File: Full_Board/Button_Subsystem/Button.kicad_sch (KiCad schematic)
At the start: 7 parts

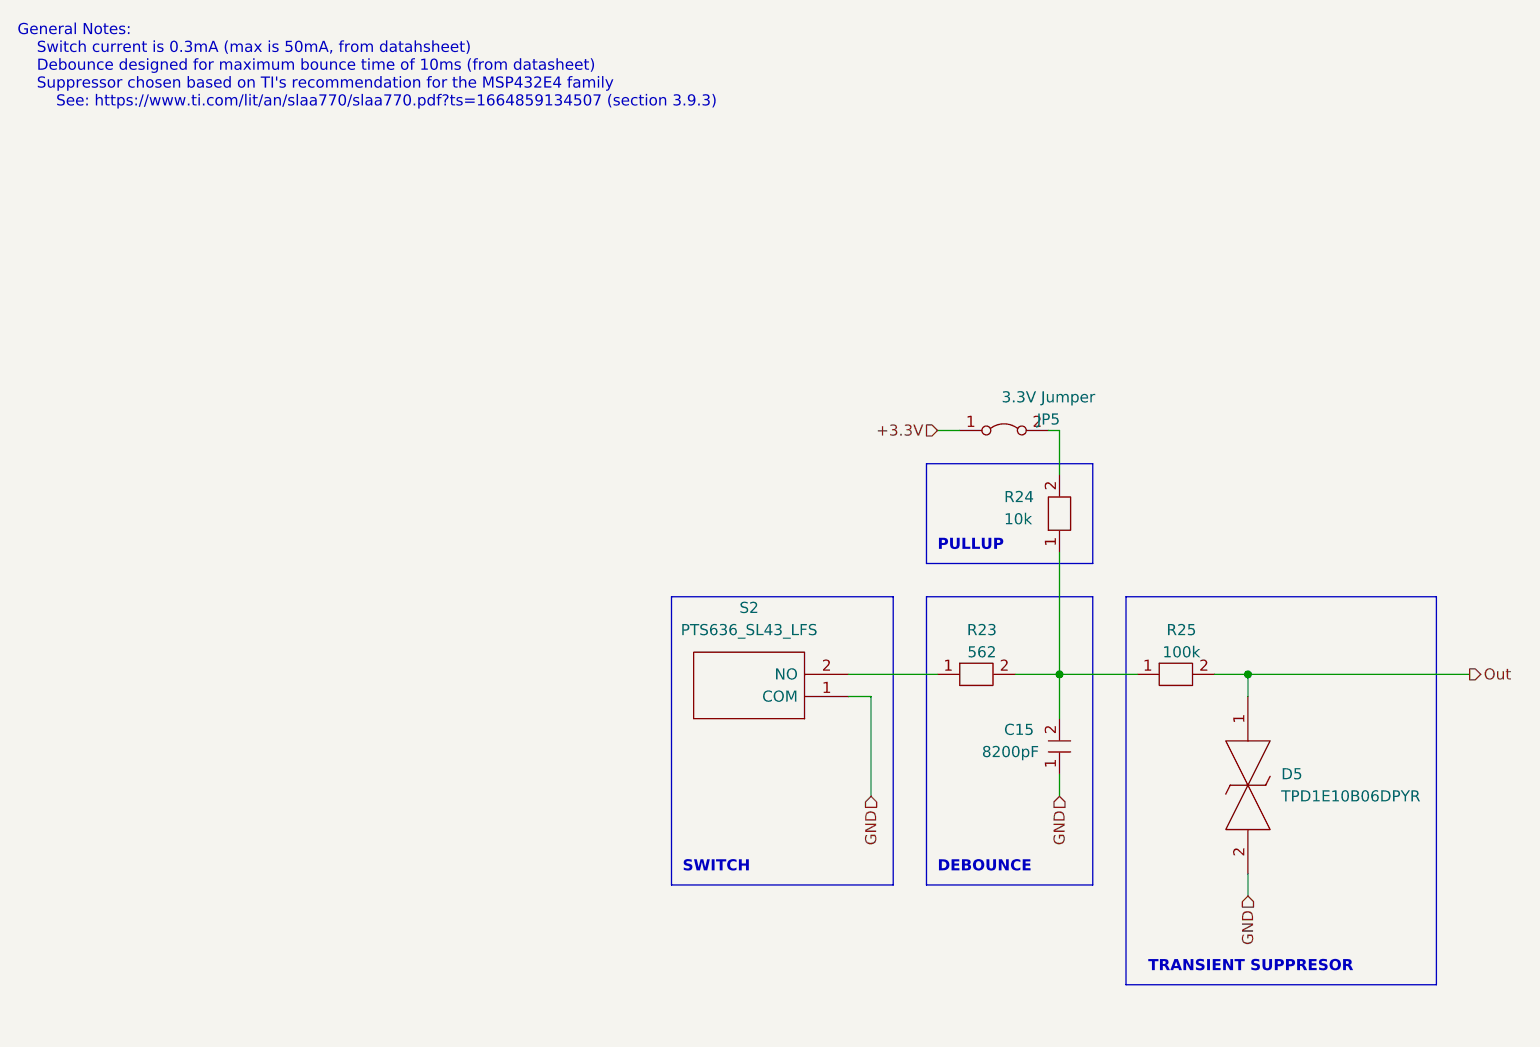
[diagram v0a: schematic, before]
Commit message: Swapped TVS Diodes
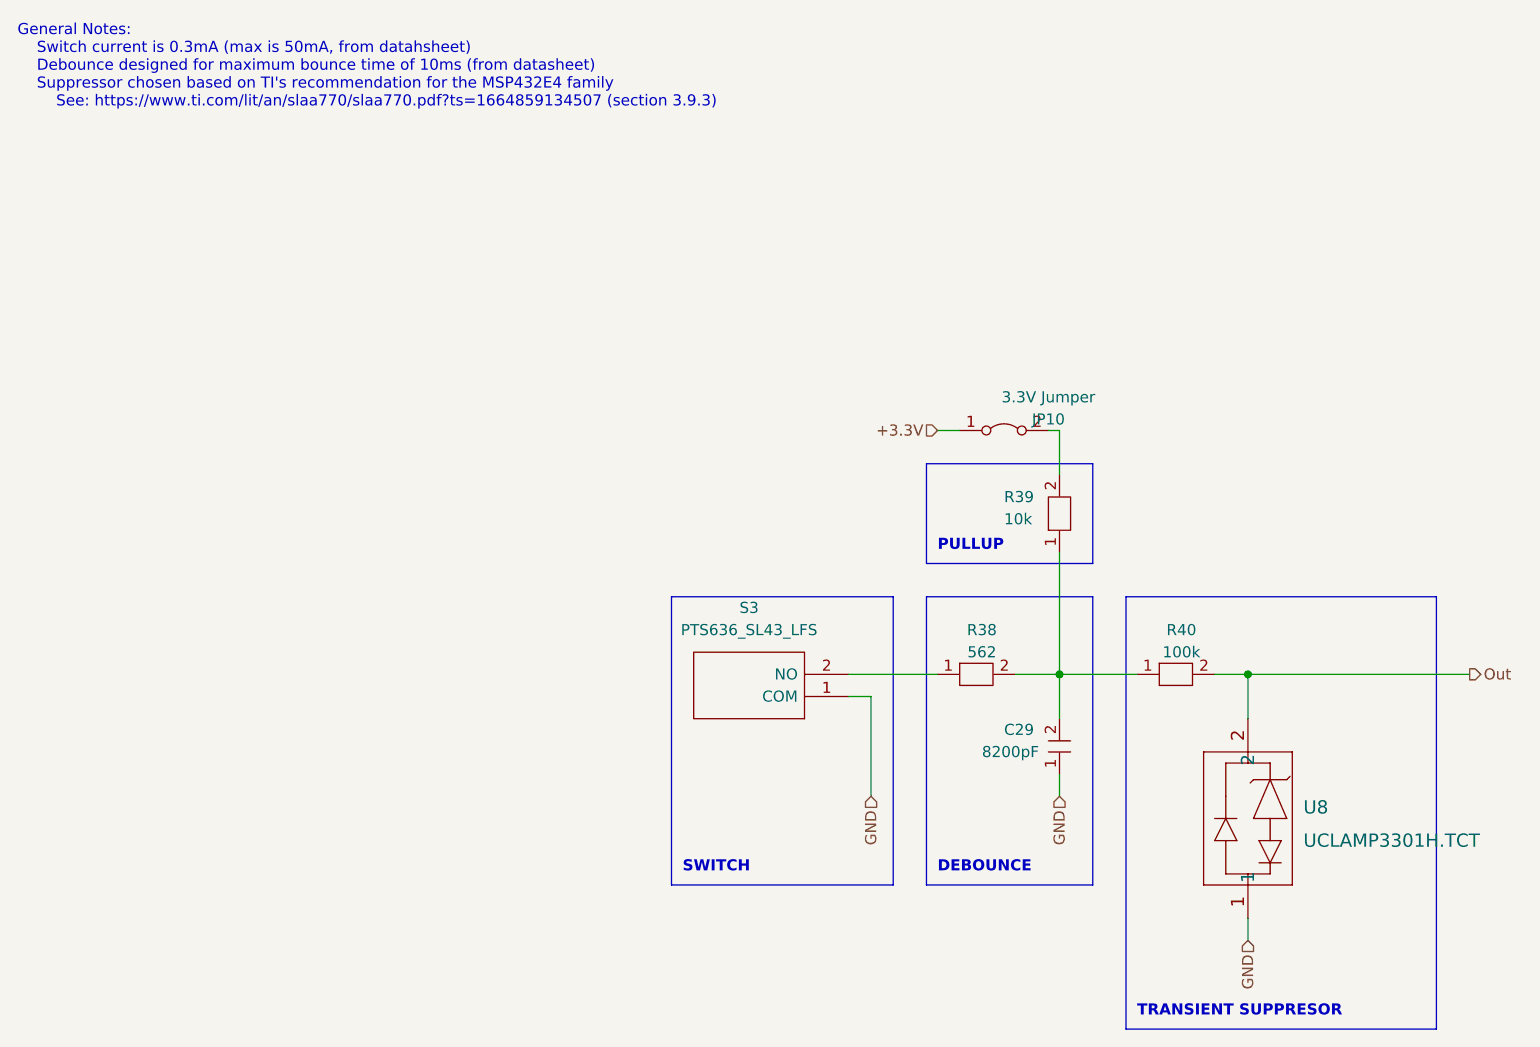
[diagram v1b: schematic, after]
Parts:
- removed D5: TPD1E10B06DPYR, TPD1E10B06DPYR:TPD1E10B06DPYR, symbol TPD1E10B06DPYR:TPD1E10B06DPYR
- added U8: UCLAMP3301H.TCT, SOD_01H.TCT_SEM, symbol UCLAMP3301H-TCT:UCLAMP3301H.TCT
- renumbered C15 to C29, JP5 to JP10, R23 to R38, R24 to R39, R25 to R40, S2 to S3
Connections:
- net GND: now also U8.1
- net Out: now also U8.2
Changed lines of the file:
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@@
     (stroke (width 0) (type default) (color 0 0 0 0))
   )
-  (polyline (pts (xy 180.34 129.54) (xy 180.34 85.09))
+  (polyline (pts (xy 180.34 134.62) (xy 180.34 85.09))
     (stroke (width 0) (type default) (color 0 0 0 0))
   )
@@
     (stroke (width 0) (type default) (color 0 0 0 0))
   )
-  (wire (pts (xy 158.75 93.98) (xy 158.75 96.52))
+  (wire (pts (xy 158.75 93.98) (xy 158.75 99.06))
     (stroke (width 0) (type default) (color 0 0 0 0))
   )
@@
     (stroke (width 0) (type default) (color 0 0 0 0))
   )
-  (polyline (pts (xy 144.78 129.54) (xy 180.34 129.54))
+  (polyline (pts (xy 144.78 134.62) (xy 180.34 134.62))
     (stroke (width 0) (type default) (color 0 0 0 0))
   )
@@
     (stroke (width 0) (type default) (color 0 0 0 0))
   )
+  (wire (pts (xy 158.75 121.92) (xy 158.75 124.46))
+    (stroke (width 0) (type default) (color 0 0 0 0))
+  )
   (polyline (pts (xy 92.71 118.11) (xy 118.11 118.11))
     (stroke (width 0) (type default) (color 0 0 0 0))
@@
     (stroke (width 0) (type default) (color 0 0 0 0))
   )
-  (polyline (pts (xy 144.78 85.09) (xy 144.78 129.54))
+  (polyline (pts (xy 144.78 85.09) (xy 144.78 134.62))
     (stroke (width 0) (type default) (color 0 0 0 0))
   )
@@
     (stroke (width 0) (type default) (color 0 0 0 0))
   )
-  (wire (pts (xy 158.75 116.84) (xy 158.75 119.38))
-    (stroke (width 0) (type default) (color 0 0 0 0))
-  )
-  (text "TRANSIENT SUPPRESOR" (at 147.32 128.27 0)
+  (text "TRANSIENT SUPPRESOR" (at 146.05 133.35 0)
     (effects (font (size 1.27 1.27) bold) (justify left bottom))
   )
@@
     (effects (font (size 1.27 1.27)) (justify right))
   )
-  (hierarchical_label "GND" (shape input) (at 158.75 119.38 270)
+  (hierarchical_label "GND" (shape input) (at 158.75 124.46 270)
     (effects (font (size 1.27 1.27)) (justify right))
   )
@@
   (symbol (lib_id "RMCF1206FT10K0:10k") (at 137.16 80.01 90)
     (in_bom yes) (on_board yes)
-    (property "Reference" "R24" (id 0) (at 130.81 73.66 90)
+    (property "Reference" "R39" (id 0) (at 130.81 73.66 90)
       (effects (font (size 1.27 1.27)) (justify right))
     )
@@
   (symbol (lib_id "C1210C822K2RACAUTO:C1210C822K2RACAUTO") (at 137.16 105.41 90)
     (in_bom yes) (on_board yes)
-    (property "Reference" "C15" (id 0) (at 130.81 100.33 90)
+    (property "Reference" "C29" (id 0) (at 130.81 100.33 90)
       (effects (font (size 1.27 1.27)) (justify right))
     )
@@
     (pin "2")
   )
+  (symbol (lib_id "UCLAMP3301H-TCT:UCLAMP3301H.TCT") (at 158.75 130.81 90)
+    (in_bom yes) (on_board yes) (fields_autoplaced)
+    (property "Reference" "U8" (id 0) (at 165.1 109.22 90)
+      (effects (font (size 1.524 1.524)) (justify right))
+    )
+    (property "Value" "UCLAMP3301H.TCT" (id 1) (at 165.1 113.03 90)
+      (effects (font (size 1.524 1.524)) (justify right))
+    )
+    (property "Footprint" "SOD_01H.TCT_SEM" (id 2) (at 152.654 110.49 0)
+      (effects (font (size 1.524 1.524)) hide)
+    )
+    (property "Datasheet" "https://semtech.my.salesforce.com/sfc/p/#E0000000JelG/a/44000000MDWf/s0KJxyOHQyYOcvBXVBK9X3X8Cxj1gNltZ2vd2k1S0Wo" (id 3) (at 158.75 130.81 0)
+      (effects (font (size 1.524 1.524)) hide)
+    )
+    (property "Manufacturers Part Number" "UCLAMP3301H.TCT" (id 4) (at 158.75 130.81 0)
+      (effects (font (size 1.27 1.27)) hide)
+    )
+    (property "Digikey Part Number" "UCLAMP3301HDKR-ND" (id 5) (at 158.75 130.81 0)
+      (effects (font (size 1.27 1.27)) hide)
+    )
+    (property "Mouser Part Number" "" (id 6) (at 158.75 130.81 0)
+      (effects (font (size 1.27 1.27)) hide)
+    )
+    (property "Digikey Link" "https://www.digikey.com/en/products/detail/semtech-corporation/UCLAMP3301H-TCT/1000952" (id 7) (at 158.75 130.81 0)
+      (effects (font (size 1.27 1.27)) hide)
+    )
+    (property "Mouser Link" "" (id 8) (at 158.75 130.81 0)
+      (effects (font (size 1.27 1.27)) hide)
+    )
+    (pin "1")
+    (pin "2")
+  )
   (symbol (lib_id "Jumper:Jumper_2_Bridged") (at 130.81 66.04 0)
     (in_bom yes) (on_board yes)
-    (property "Reference" "JP5" (id 0) (at 135.89 64.77 0))
+    (property "Reference" "JP10" (id 0) (at 135.89 64.77 0))
     (property "Value" "3.3V Jumper" (id 1) (at 135.89 62.23 0))
     (property "Footprint" "TestPoint:TestPoint_2Pads_Pitch2.54mm_Drill0.8mm" (id 2) (at 130.81 66.04 0)
@@
   (symbol (lib_id "CR0402-FX-5620GLF:CR0402-FX-5620GLF") (at 123.19 93.98 0)
     (in_bom yes) (on_board yes)
-    (property "Reference" "R23" (id 0) (at 128.27 88.9 0))
+    (property "Reference" "R38" (id 0) (at 128.27 88.9 0))
     (property "Value" "562" (id 1) (at 128.27 91.44 0))
     (property "Footprint" "CR0402-FX-5620GLF:RESC1005X40N" (id 2) (at 137.16 92.71 0)
@@
   (symbol (lib_id "RCV2512100KFKEGAT:RCV2512100KFKEGAT") (at 146.05 93.98 0)
     (in_bom yes) (on_board yes)
-    (property "Reference" "R25" (id 0) (at 151.13 88.9 0))
+    (property "Reference" "R40" (id 0) (at 151.13 88.9 0))
     (property "Value" "100k" (id 1) (at 151.13 91.44 0))
     (property "Footprint" "RCV2512100KFKEGAT:RESC6332X70N" (id 2) (at 160.02 92.71 0)
@@
   (symbol (lib_id "PTS636_SL43_LFS:PTS636_SL43_LFS") (at 113.03 96.52 180)
     (in_bom yes) (on_board yes) (fields_autoplaced)
-    (property "Reference" "S2" (id 0) (at 101.6 86.36 0))
+    (property "Reference" "S3" (id 0) (at 101.6 86.36 0))
     (property "Value" "PTS636_SL43_LFS" (id 1) (at 101.6 88.9 0))
     (property "Footprint" "PTS636_SL43_LFS:PTS636SL43LFS" (id 2) (at 93.98 99.06 0)
@@
     )
     (pin "1")
-    (pin "2")
-  )
-  (symbol (lib_id "TPD1E10B06DPYR:TPD1E10B06DPYR") (at 158.75 96.52 270)
-    (in_bom yes) (on_board yes)
-    (property "Reference" "D5" (id 0) (at 162.56 105.41 90)
-      (effects (font (size 1.27 1.27)) (justify left))
-    )
-    (property "Value" "TPD1E10B06DPYR" (id 1) (at 162.56 107.9499 90)
-      (effects (font (size 1.27 1.27)) (justify left))
-    )
-    (property "Footprint" "TPD1E10B06DPYR:TPD1E10B06DPYR" (id 2) (at 162.56 109.22 0)
-      (effects (font (size 1.27 1.27)) (justify left bottom) hide)
-    )
-    (property "Datasheet" "https://www.ti.com/lit/ds/symlink/tpd1e10b06.pdf?HQS=dis-mous-null-mousermode-dsf-pf-null-wwe&ts=1664782336823&ref_url=https%253A%252F%252Feu.mouser.com%252F" (id 3) (at 160.02 109.22 0)
-      (effects (font (size 1.27 1.27)) (justify left bottom) hide)
-    )
-    (property "Manufacturer's Part Number" "TPD1E10B06DPYR" (id 4) (at 144.78 109.22 0)
-      (effects (font (size 1.27 1.27)) (justify left bottom) hide)
-    )
-    (property "Digikey Part Number" "296-30406-1-ND" (id 5) (at 157.48 109.22 0)
-      (effects (font (size 1.27 1.27)) (justify left bottom) hide)
-    )
-    (property "Mouser Part Number" "595-TPD1E10B06DPYR" (id 6) (at 152.4 109.22 0)
-      (effects (font (size 1.27 1.27)) (justify left bottom) hide)
-    )
-    (property "Digikey link" "https://www.digikey.com/en/products/detail/texas-instruments/TPD1E10B06DPYR/3197744" (id 7) (at 149.86 109.22 0)
-      (effects (font (size 1.27 1.27)) (justify left bottom) hide)
-    )
-    (property "Mouser link" "https://www.mouser.com/ProductDetail/Texas-Instruments/TPD1E10B06DPYR?qs=UFc95S4Z4CaJYpQ4xqTc0g%3D%3D" (id 8) (at 147.32 109.22 0)
-      (effects (font (size 1.27 1.27)) (justify left bottom) hide)
-    )
-    (pin "1")

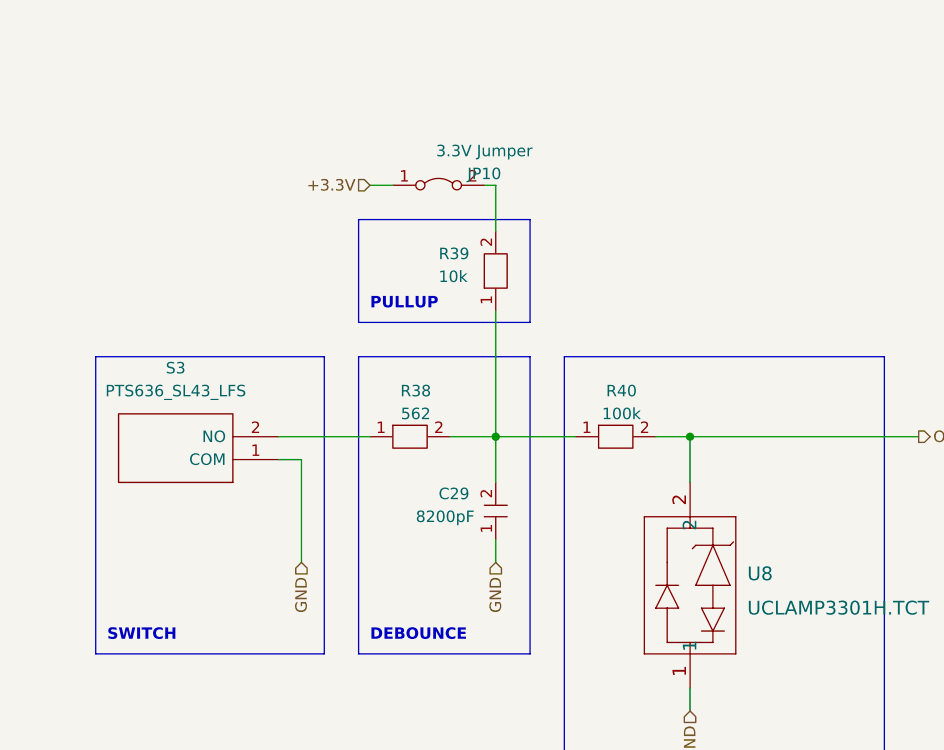
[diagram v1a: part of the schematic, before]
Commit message: Relayed out the power supply and stepper drivers
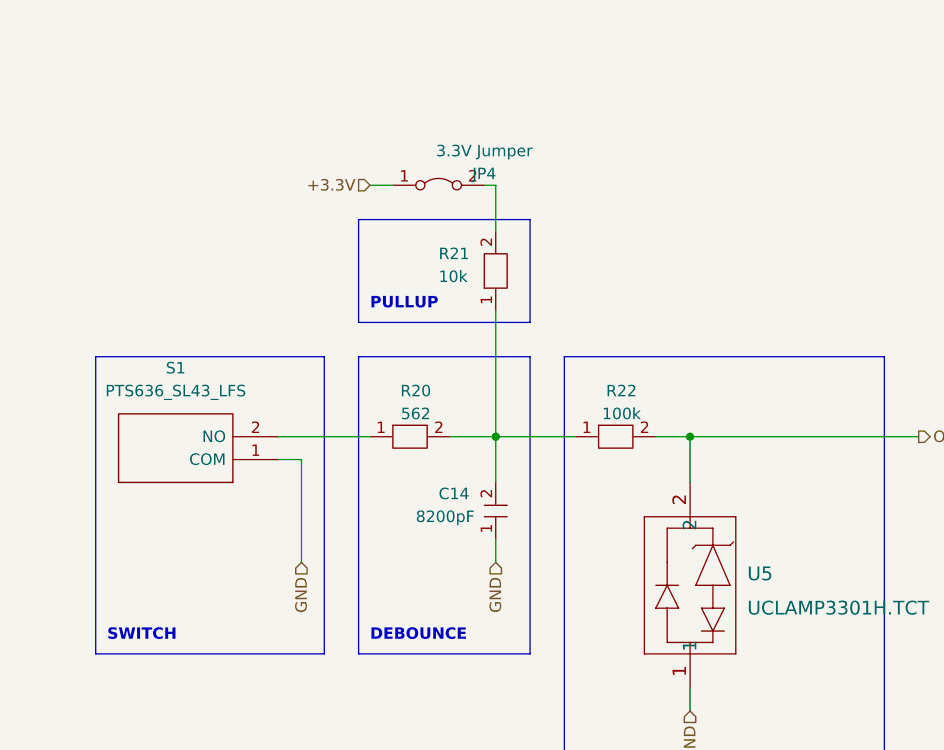
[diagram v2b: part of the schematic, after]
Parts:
- U5: renamed from U8; footprint SOD_01H.TCT_SEM -> UCLAMP3310H-TCT:UCLAMP3301H.TCT
- renumbered C29 to C14, JP10 to JP4, R38 to R20, R39 to R21, R40 to R22, S3 to S1
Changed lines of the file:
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@@
   (symbol (lib_id "RMCF1206FT10K0:10k") (at 137.16 80.01 90)
     (in_bom yes) (on_board yes)
-    (property "Reference" "R39" (id 0) (at 130.81 73.66 90)
+    (property "Reference" "R21" (id 0) (at 130.81 73.66 90)
       (effects (font (size 1.27 1.27)) (justify right))
     )
@@
   (symbol (lib_id "C1210C822K2RACAUTO:C1210C822K2RACAUTO") (at 137.16 105.41 90)
     (in_bom yes) (on_board yes)
-    (property "Reference" "C29" (id 0) (at 130.81 100.33 90)
+    (property "Reference" "C14" (id 0) (at 130.81 100.33 90)
       (effects (font (size 1.27 1.27)) (justify right))
     )
@@
   (symbol (lib_id "UCLAMP3301H-TCT:UCLAMP3301H.TCT") (at 158.75 130.81 90)
     (in_bom yes) (on_board yes) (fields_autoplaced)
-    (property "Reference" "U8" (id 0) (at 165.1 109.22 90)
+    (property "Reference" "U5" (id 0) (at 165.1 109.22 90)
       (effects (font (size 1.524 1.524)) (justify right))
     )
@@
       (effects (font (size 1.524 1.524)) (justify right))
     )
-    (property "Footprint" "SOD_01H.TCT_SEM" (id 2) (at 152.654 110.49 0)
+    (property "Footprint" "UCLAMP3310H-TCT:UCLAMP3301H.TCT" (id 2) (at 152.654 110.49 0)
       (effects (font (size 1.524 1.524)) hide)
     )
@@
   (symbol (lib_id "Jumper:Jumper_2_Bridged") (at 130.81 66.04 0)
     (in_bom yes) (on_board yes)
-    (property "Reference" "JP10" (id 0) (at 135.89 64.77 0))
+    (property "Reference" "JP4" (id 0) (at 135.89 64.77 0))
     (property "Value" "3.3V Jumper" (id 1) (at 135.89 62.23 0))
     (property "Footprint" "TestPoint:TestPoint_2Pads_Pitch2.54mm_Drill0.8mm" (id 2) (at 130.81 66.04 0)
@@
   (symbol (lib_id "CR0402-FX-5620GLF:CR0402-FX-5620GLF") (at 123.19 93.98 0)
     (in_bom yes) (on_board yes)
-    (property "Reference" "R38" (id 0) (at 128.27 88.9 0))
+    (property "Reference" "R20" (id 0) (at 128.27 88.9 0))
     (property "Value" "562" (id 1) (at 128.27 91.44 0))
     (property "Footprint" "CR0402-FX-5620GLF:RESC1005X40N" (id 2) (at 137.16 92.71 0)
@@
   (symbol (lib_id "RCV2512100KFKEGAT:RCV2512100KFKEGAT") (at 146.05 93.98 0)
     (in_bom yes) (on_board yes)
-    (property "Reference" "R40" (id 0) (at 151.13 88.9 0))
+    (property "Reference" "R22" (id 0) (at 151.13 88.9 0))
     (property "Value" "100k" (id 1) (at 151.13 91.44 0))
     (property "Footprint" "RCV2512100KFKEGAT:RESC6332X70N" (id 2) (at 160.02 92.71 0)
@@
   (symbol (lib_id "PTS636_SL43_LFS:PTS636_SL43_LFS") (at 113.03 96.52 180)
     (in_bom yes) (on_board yes) (fields_autoplaced)
-    (property "Reference" "S3" (id 0) (at 101.6 86.36 0))
+    (property "Reference" "S1" (id 0) (at 101.6 86.36 0))
     (property "Value" "PTS636_SL43_LFS" (id 1) (at 101.6 88.9 0))
     (property "Footprint" "PTS636_SL43_LFS:PTS636SL43LFS" (id 2) (at 93.98 99.06 0)

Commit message: More layout work
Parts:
- renumbered C14 to C15, JP4 to JP5, R20 to R23, R21 to R24, R22 to R25, S1 to S2, U5 to U6
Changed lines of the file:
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@@
   (symbol (lib_id "RMCF1206FT10K0:10k") (at 137.16 80.01 90)
     (in_bom yes) (on_board yes)
-    (property "Reference" "R21" (id 0) (at 130.81 73.66 90)
+    (property "Reference" "R24" (id 0) (at 130.81 73.66 90)
       (effects (font (size 1.27 1.27)) (justify right))
     )
@@
   (symbol (lib_id "C1210C822K2RACAUTO:C1210C822K2RACAUTO") (at 137.16 105.41 90)
     (in_bom yes) (on_board yes)
-    (property "Reference" "C14" (id 0) (at 130.81 100.33 90)
+    (property "Reference" "C15" (id 0) (at 130.81 100.33 90)
       (effects (font (size 1.27 1.27)) (justify right))
     )
@@
   (symbol (lib_id "UCLAMP3301H-TCT:UCLAMP3301H.TCT") (at 158.75 130.81 90)
     (in_bom yes) (on_board yes) (fields_autoplaced)
-    (property "Reference" "U5" (id 0) (at 165.1 109.22 90)
+    (property "Reference" "U6" (id 0) (at 165.1 109.22 90)
       (effects (font (size 1.524 1.524)) (justify right))
     )
@@
   (symbol (lib_id "Jumper:Jumper_2_Bridged") (at 130.81 66.04 0)
     (in_bom yes) (on_board yes)
-    (property "Reference" "JP4" (id 0) (at 135.89 64.77 0))
+    (property "Reference" "JP5" (id 0) (at 135.89 64.77 0))
     (property "Value" "3.3V Jumper" (id 1) (at 135.89 62.23 0))
     (property "Footprint" "TestPoint:TestPoint_2Pads_Pitch2.54mm_Drill0.8mm" (id 2) (at 130.81 66.04 0)
@@
   (symbol (lib_id "CR0402-FX-5620GLF:CR0402-FX-5620GLF") (at 123.19 93.98 0)
     (in_bom yes) (on_board yes)
-    (property "Reference" "R20" (id 0) (at 128.27 88.9 0))
+    (property "Reference" "R23" (id 0) (at 128.27 88.9 0))
     (property "Value" "562" (id 1) (at 128.27 91.44 0))
     (property "Footprint" "CR0402-FX-5620GLF:RESC1005X40N" (id 2) (at 137.16 92.71 0)
@@
   (symbol (lib_id "RCV2512100KFKEGAT:RCV2512100KFKEGAT") (at 146.05 93.98 0)
     (in_bom yes) (on_board yes)
-    (property "Reference" "R22" (id 0) (at 151.13 88.9 0))
+    (property "Reference" "R25" (id 0) (at 151.13 88.9 0))
     (property "Value" "100k" (id 1) (at 151.13 91.44 0))
     (property "Footprint" "RCV2512100KFKEGAT:RESC6332X70N" (id 2) (at 160.02 92.71 0)
@@
   (symbol (lib_id "PTS636_SL43_LFS:PTS636_SL43_LFS") (at 113.03 96.52 180)
     (in_bom yes) (on_board yes) (fields_autoplaced)
-    (property "Reference" "S1" (id 0) (at 101.6 86.36 0))
+    (property "Reference" "S2" (id 0) (at 101.6 86.36 0))
     (property "Value" "PTS636_SL43_LFS" (id 1) (at 101.6 88.9 0))
     (property "Footprint" "PTS636_SL43_LFS:PTS636SL43LFS" (id 2) (at 93.98 99.06 0)
